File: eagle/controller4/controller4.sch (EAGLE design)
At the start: 64 parts, among them Q1 check_pins, Q2 FDD4141TO252, Q3 check_pins, X1 1501_04

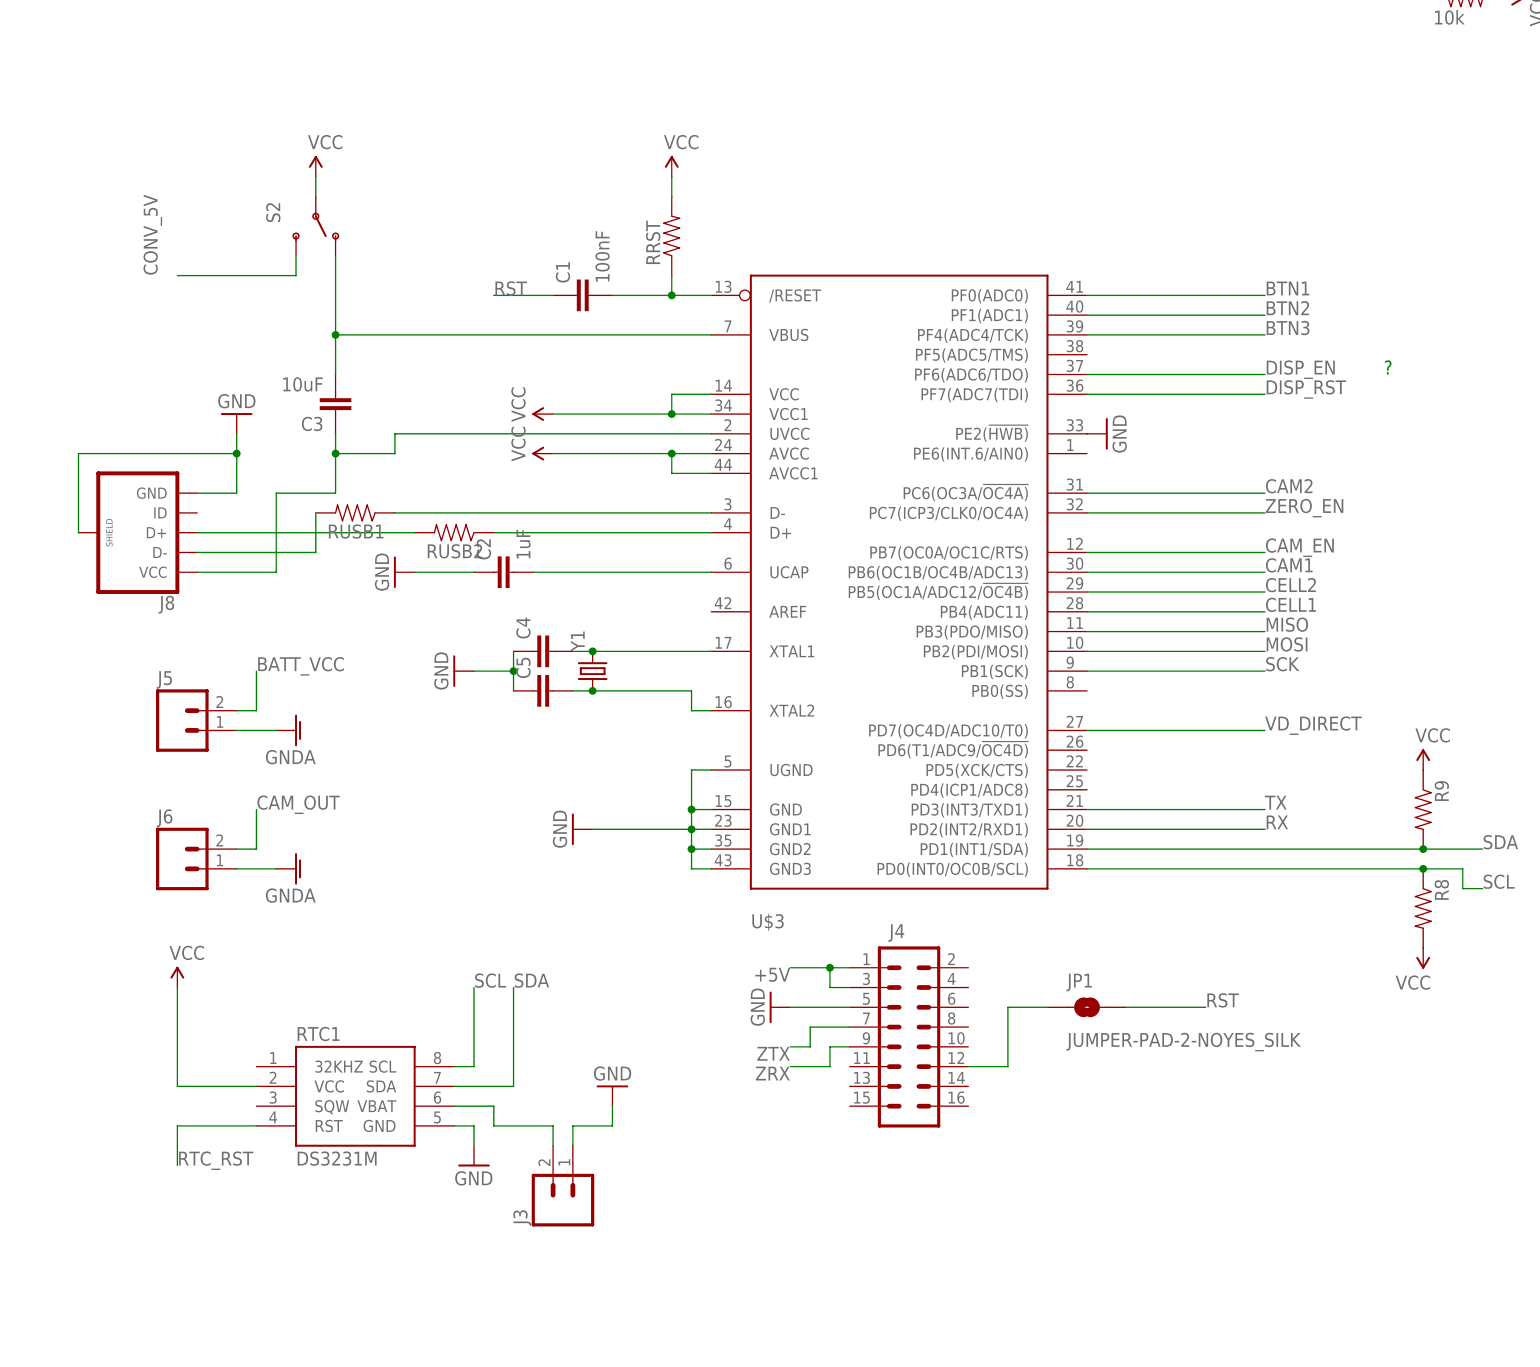
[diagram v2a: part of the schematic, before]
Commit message: controller4: changed layout
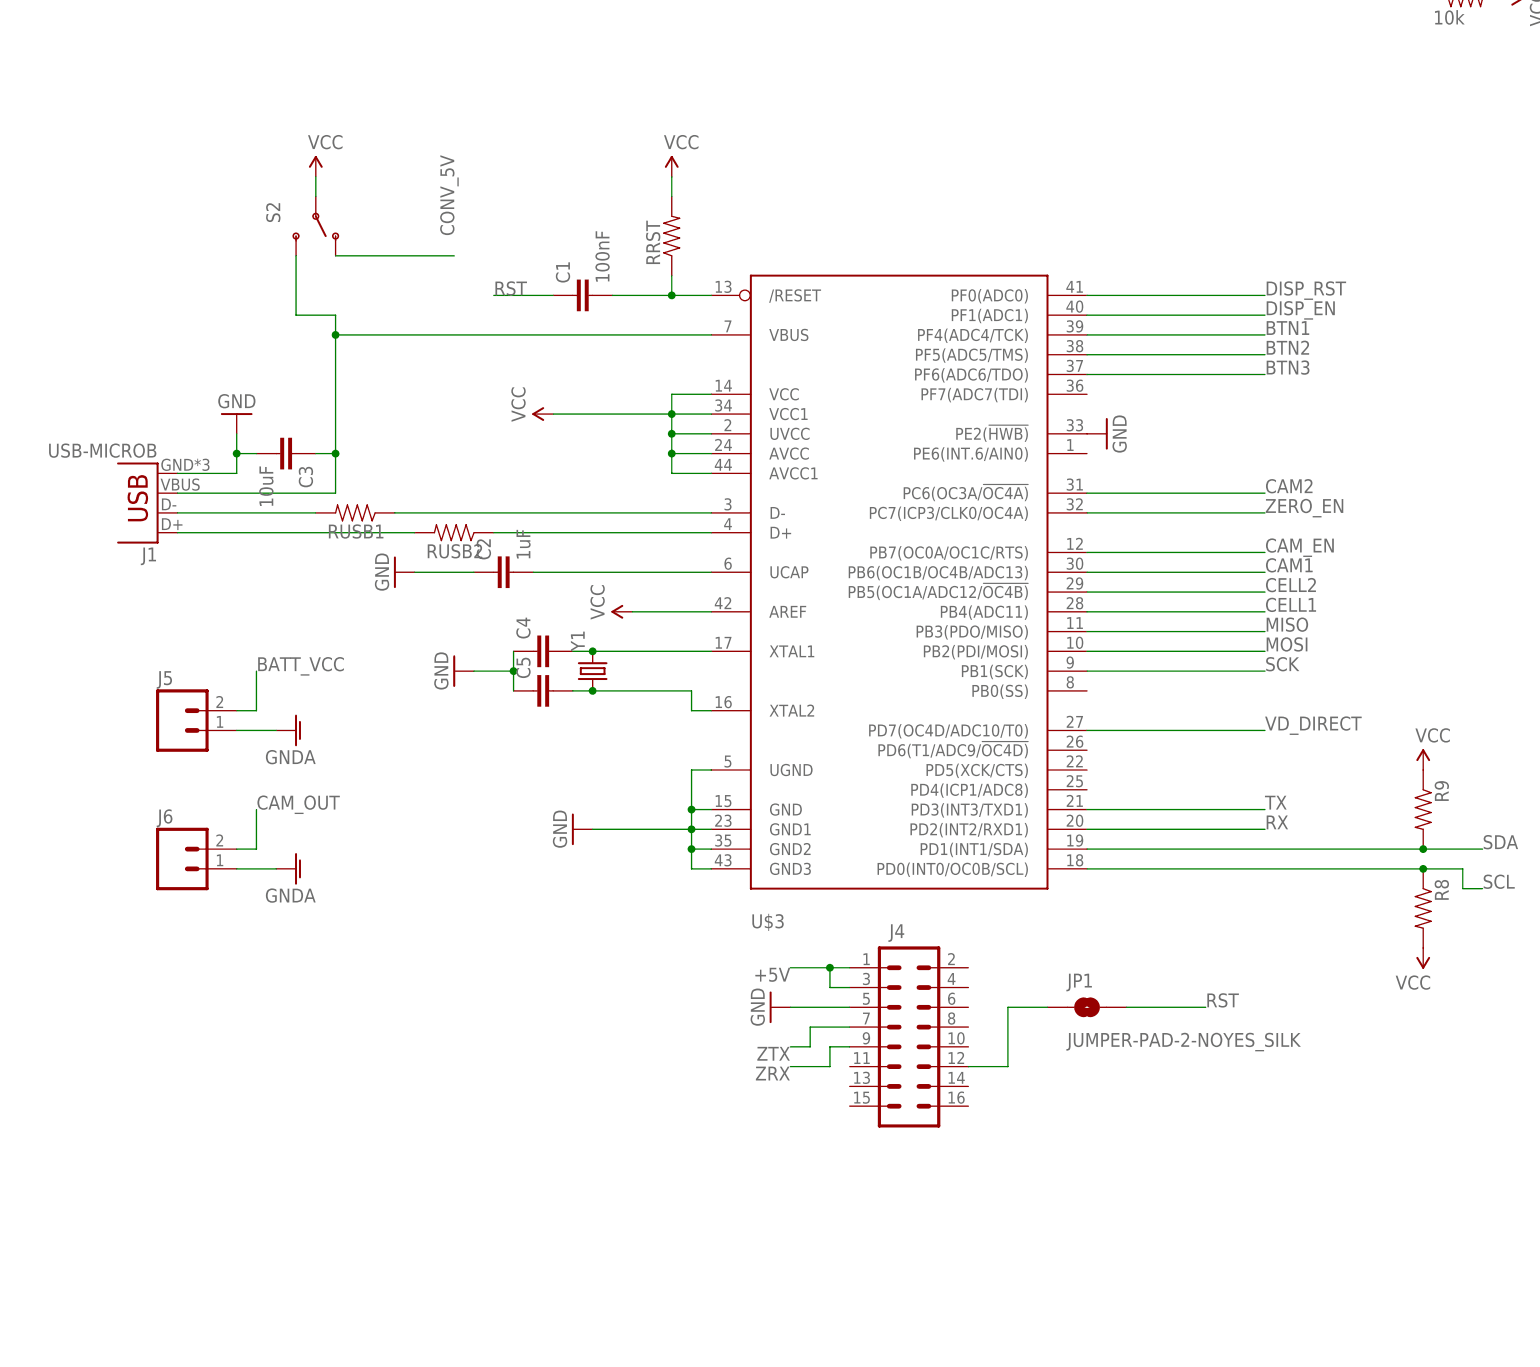
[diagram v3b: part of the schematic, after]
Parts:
- removed J3: (no value), SparkFun-Connectors:M02LOCK_LONGPADS
- removed J8: (no value), SparkFun-Connectors:USB_MICROB_PLUGCONN-11752
- removed RTC1: DS3231M, SparkFun-DigitalIC:DS3231M
- added J1: USB-MICROB, SparkFun-Connectors:USB-MICROB
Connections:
- removed net N$10: C3.2, S2.O, U$3.VBUS
- removed net N$25: J3.2, RTC1.VBAT
- removed net RTC_RST: RTC1.RST
- net BTN1: now also U$3.PF4(ADC4/TCK); no longer U$3.PF0(ADC0)
- net BTN2: now also U$3.PF5(ADC5/TMS); no longer U$3.PF1(ADC1)
- net BTN3: now also U$3.PF6(ADC6/TDO); no longer U$3.PF4(ADC4/TCK)
- net CONV_5V: now also S2.O; no longer S2.S
- net DISP_EN: now also U$3.PF1(ADC1); no longer U$3.PF6(ADC6/TDO)
- net DISP_RST: now also U$3.PF0(ADC0); no longer U$3.PF7(ADC7(TDI)
- net GND: now also C3.2, J1.GND; no longer J3.1, J8.GND, J8.SHIELD, RTC1.GND
- net N$11: now also J1.D-; no longer J8.D-
- net N$14: now also J1.D+; no longer J8.D+
- net N$22: now also J1.VBUS, S2.S, U$3.VBUS; no longer J8.VCC, U$3.UVCC
- net SCL: no longer RTC1.SCL
- net SDA: no longer RTC1.SDA
- net VCC: now also Q1.E, U$3.AREF, U$3.UVCC; no longer RTC1.VCC
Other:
- note removed: "?"
- moved on the sheet: C3

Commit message: controller4: moved display to the upper half
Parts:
- removed J1: USB-MICROB, SparkFun-Connectors:USB-MICROB
- added U$1: USB-CON-5PIN-105017-0001, GeekAmmo:USB-CON-5PIN-105017-0001
- R17: value 1k -> 10k
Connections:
- net CELL1: now also U$3.PB5(OC1A/ADC12/!OC4B), VD1.2, VD2.1; no longer U$3.PB4(ADC11), VD3.2, VD4.1
- net CELL2: now also U$3.PB4(ADC11), VD3.2, VD4.1; no longer U$3.PB5(OC1A/ADC12/!OC4B), VD1.2, VD2.1
- net DISP_EN: now also U$3.PD6(T1/ADC9/!OC4D); no longer U$3.PF1(ADC1)
- net DISP_RST: now also U$3.PD4(ICP1/ADC8); no longer U$3.PF0(ADC0)
- net GND: now also U$1.GND; no longer J1.GND
- net N$11: now also U$1.D-; no longer J1.D-
- net N$14: now also U$1.D+; no longer J1.D+
- net N$22: now also U$1.VBUS; no longer J1.VBUS
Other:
- note added: "changed pull up resistor from 1k to 10k."

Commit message: controller4: intermediate
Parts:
- removed BTN_DW, BTN_UP, BTN_X: (no value), SparkFun-Retired:TAC_SWITCHPTH
- added RB4, RB5: 10k, SparkFun-Resistors:RESISTOR1206
- added S1: (no value), SparkFun-Electromechanical:JOYSTICK_MINI
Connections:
- removed net BTN1: BTN_UP.4, RB1.1, U$3.PF4(ADC4/TCK)
- removed net BTN2: BTN_DW.4, RB2.1, U$3.PF5(ADC5/TMS)
- removed net BTN3: BTN_X.4, RB3.1, U$3.PF6(ADC6/TDO)
- new net BTN_C: RB3.1, S1.CENT, U$3.PF4(ADC4/TCK)
- new net BTN_D: RB1.1, S1.DOWN, U$3.PF7(ADC7(TDI)
- new net BTN_L: RB4.1, S1.LEFT, U$3.PF5(ADC5/TMS)
- new net BTN_R: RB5.1, S1.RIGHT, U$3.PF6(ADC6/TDO)
- new net BTN_U: RB2.1, S1.UP, U$3.PF1(ADC1)
- new net FOO: U$3.PC7(ICP3/CLK0/OC4A)
- net CAM_EN: now also U$3.PF0(ADC0); no longer U$3.PB7(OC0A/OC1C/RTS)
- net GND: now also S1.GND; no longer BTN_DW.2, BTN_UP.2, BTN_X.2
- net VCC: now also RB4.2, RB5.2
- net ZERO_EN: now also U$3.PB7(OC0A/OC1C/RTS); no longer U$3.PC7(ICP3/CLK0/OC4A)
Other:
- moved on the sheet: RB1, RB2, RB3

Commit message: controller4: eagle files nearly finished
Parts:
- removed H3: MOUNT-HOLE2.8, holes:MOUNT-HOLE2.8
- removed J4: (no value), SparkFun-Connectors:M08X2
- removed JP1: JUMPER-PAD-2-NOYES_SILK, SparkFun-Passives:JUMPER-PAD-2-NOYES_SILK
- removed U$1: USB-CON-5PIN-105017-0001, GeekAmmo:USB-CON-5PIN-105017-0001
- added D1: 1N4004, adafruit:1N4004
- added D2: (no value), SparkFun-LED:WS2812B
- added J1: (no value), SparkFun-Connectors:M02LOCK_LONGPADS
- added J3: (no value), SparkFun-Connectors:M10X2
- added JP2: JUMPER-PAD-2-NOYES_SILK, SparkFun-Passives:JUMPER-PAD-2-NOYES_SILK
- added R2: (no value), SparkFun-Resistors:RESISTOR1206
- added RTC1: DS3231M, SparkFun-DigitalIC:DS3231M
- added R_LED: UNKNOWN, SparkFun-Resistors:RESISTOR1206
- added SH1: SHORT-HT5, shorts-old:SHORT-HT5
- added TP1: TPB1,27, testpad:TPB1,27
- added T_ZERO_N: (no value), SparkFun-DiscreteSemi:TRANSISTOR_NPN2N3904
- added X2: ZX62D-B-5PA8, zx62d-b-5pa8-oshpark_10:ZX62D-B-5PA8
- C4, C5: value (none) -> 22pF
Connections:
- removed net FOO: U$3.PC7(ICP3/CLK0/OC4A)
- new net LED: R_LED.1, U$3.PC7(ICP3/CLK0/OC4A)
- new net N$10: RUSB1.2, X2G$1.2
- new net N$13: J3.12, JP2.1
- new net N$16: D1.A, Q2.D
- new net N$18: R10.2, T_ZERO_N.C
- new net VBAT: J1.1, RTC1.VBAT
- net +5V: now also J3.1, J3.3; no longer J4.1, J4.3
- net BTN_C: now also U$3.PF0(ADC0); no longer U$3.PF4(ADC4/TCK)
- net BTN_D: now also U$3.PF6(ADC6/TDO); no longer U$3.PF7(ADC7(TDI)
- net BTN_L: now also U$3.PF1(ADC1); no longer U$3.PF5(ADC5/TMS)
- net BTN_R: now also U$3.PF5(ADC5/TMS); no longer U$3.PF6(ADC6/TDO)
- net BTN_U: now also U$3.PF4(ADC4/TCK); no longer U$3.PF1(ADC1)
- net CAM_EN: now also U$3.PF7(ADC7(TDI); no longer U$3.PF0(ADC0)
- net CAM_OUT: now also D1.C; no longer Q2.D
- net CELL1: now also U$3.PB4(ADC11); no longer U$3.PB5(OC1A/ADC12/!OC4B)
- net CELL2: now also U$3.PD7(OC4D/ADC10/T0); no longer U$3.PB4(ADC11)
- net GND: now also D2.VSS, J1.2, J3.5, RTC1.GND, SH1.P$1, TP1.TP, T_ZERO_N.E, X2G$1.5; no longer J4.5, U$1.GND
- net GNDA: now also SH1.P$2
- net N$11: now also RUSB2.2, X2G$1.3; no longer RUSB1.2, U$1.D-
- net N$14: now also R2.1, T_ZERO_N.B; no longer RUSB2.2, U$1.D+
- net N$22: now also X2G$1.1; no longer U$1.VBUS
- net N$7: now also D2.DIN, R_LED.2; no longer J4.12, JP1.1
- net RST: now also JP2.2; no longer JP1.2
- net SCL: now also RTC1.SCL
- net SDA: now also RTC1.SDA
- net VCC: now also D2.VDD, RTC1.VCC
- net VD_DIRECT: now also U$3.PB5(OC1A/ADC12/!OC4B); no longer U$3.PD7(OC4D/ADC10/T0)
- net ZERO_EN: now also R2.2; no longer R10.2
- net ZRX: now also J3.9; no longer J4.9
- net ZTX: now also J3.7; no longer J4.7
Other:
- note added: "TEST THAT"
- moved on the sheet: H4

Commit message: controller4: fixed remaining airwires
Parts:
- Q3: value check_pins -> (none)
- R16: value high ohm value -> 10k
- R20, R21: value (none) -> 1k
- R_LED: value UNKNOWN -> 4.7k
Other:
- note added: "VCC?"
